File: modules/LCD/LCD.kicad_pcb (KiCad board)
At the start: 2 copper layers, 40.6 x 40.6 mm, 11 parts, among them J1 Conn_01x10_Male, J2 Conn_01x10_Male

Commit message: LCD shield in work
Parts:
- removed H5, H6, H7, H8: MountingHole, MountingHole:MountingHole_3.2mm_M3
- added RV1: R_POT, Potentiometer_THT:Potentiometer_ACP_CA9-V10_Vertical, F.Cu at (72.4, 49.5)
- DS1: footprint Display:WC1602A -> CommonLibrary:WH1602-2-holes
- moved DS1 86.2 mm to (78.5, 31.2)
- moved H2 80.4 mm to (148.0, 29.2), turned to 90 degrees
- moved H4 78.7 mm to (73.0, 29.2), turned to 90 degrees
- moved H1 55.8 mm to (148.0, 62.2), turned to 90 degrees
- moved H3 53.3 mm to (73.0, 62.2), turned to 90 degrees
- moved J2 31.0 mm to (120.0, 29.2), turned to 90 degrees
- moved J1 14.8 mm to (78.1, 62.2), turned to 90 degrees
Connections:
- DS1 pad 1: Net-(DS1-Pad1) -> GND
- DS1 pad 15: Net-(DS1-Pad15) -> VCC
- DS1 pad 16: Net-(DS1-Pad16) -> GND
- DS1 pad 2: Net-(DS1-Pad2) -> VCC
- DS1 pad 5: Net-(DS1-Pad5) -> GND
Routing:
- net GND: track 0.00 -> 99.1 mm, vias 0 -> 2
- net /2: track 0.00 -> 72.9 mm
- net VCC: track 0.00 -> 70.1 mm
- net /7: track 0.00 -> 61.1 mm, vias 0 -> 2
- net /8: track 0.00 -> 48.4 mm
- net /9: track 0.00 -> 41.2 mm
- net /10: track 0.00 -> 33.2 mm
- net /11: track 0.00 -> 25.5 mm
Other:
- board size 40.6 x 40.6 mm -> 82.5 x 40.6 mm

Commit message: LCD is ready
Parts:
- RV1: footprint Potentiometer_THT:Potentiometer_ACP_CA9-V10_Vertical -> CommonLibrary:pot-5x5
- moved RV1 6.16 mm to (73.7, 43.5), turned to 270 degrees
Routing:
- net Net-(DS1-Pad3): track 0.00 -> 18.8 mm
- net VCC: track 70.1 -> 84.2 mm
- net GND: track 99.1 -> 111.7 mm
- net /2: track 72.9 -> 77.5 mm
- net /7: track 61.1 -> 61.6 mm

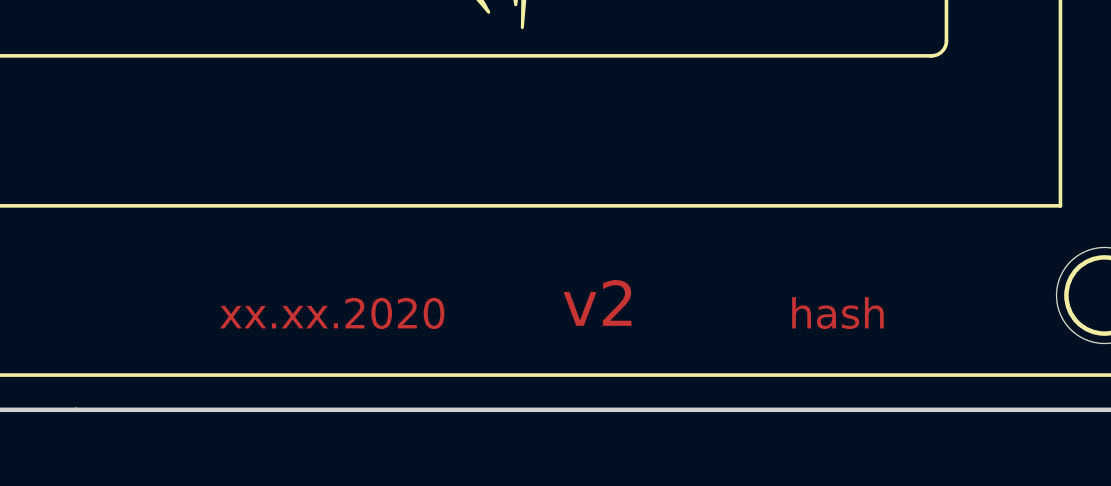
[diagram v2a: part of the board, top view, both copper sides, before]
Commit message: LCD. Add photomask in pdf.
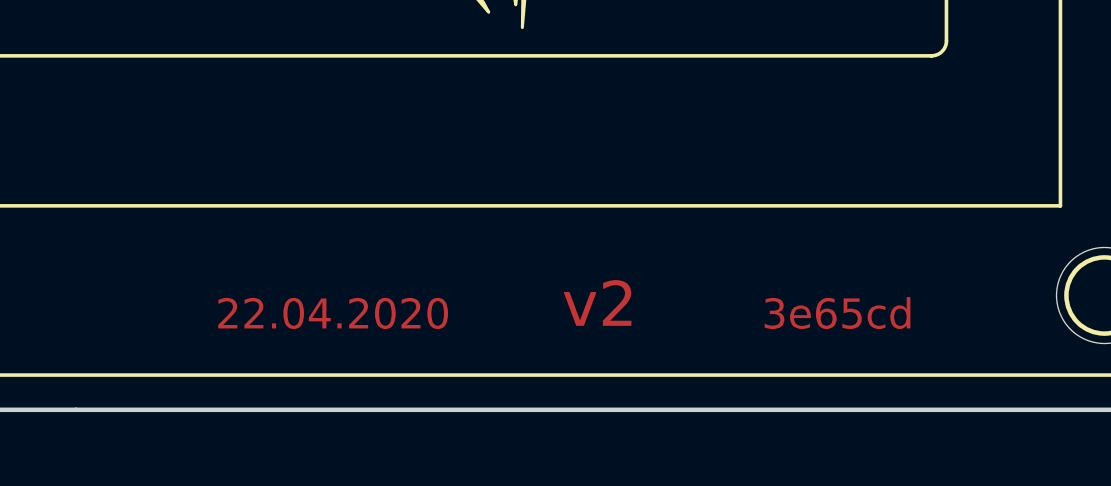
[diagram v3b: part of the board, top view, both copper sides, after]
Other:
- board text added: "22.04.2020"
- board text added: "3e65cd"
- board text removed: "hash"
- board text removed: "xx.xx.2020"
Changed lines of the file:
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@@
   )
   (setup
-    (last_trace_width 0.8)
+    (last_trace_width 0.25)
     (user_trace_width 0.6)
     (user_trace_width 0.8)
@@
     (visible_elements 7FFFFFFF)
     (pcbplotparams
-      (layerselection 0x010fc_ffffffff)
+      (layerselection 0x00000_fffffffe)
       (usegerberextensions false)
       (usegerberattributes false)
@@
       (hpglpenspeed 20)
       (hpglpendiameter 15.000000)
-      (psnegative false)
+      (psnegative true)
       (psa4output false)
       (plotreference true)
@@
       (padsonsilk false)
       (subtractmaskfromsilk false)
-      (outputformat 1)
+      (outputformat 4)
       (mirror false)
       (drillshape 1)
       (scaleselection 1)
-      (outputdirectory ""))
+      (outputdirectory "pdf/"))
   )
   (net 0 "")
@@
       (net 10 GND))
   )
-  (gr_text hash (at 139.065 62.865) (layer F.Cu)
+  (gr_text 3e65cd (at 139.065 62.865) (layer F.Cu)
     (effects (font (size 1 1) (thickness 0.2)))
   )
@@
     (effects (font (size 1.5 1.5) (thickness 0.3)))
   )
-  (gr_text xx.xx.2020 (at 122.2375 62.865) (layer F.Cu)
+  (gr_text 22.04.2020 (at 122.2375 62.865) (layer F.Cu)
     (effects (font (size 1 1) (thickness 0.2)))
   )

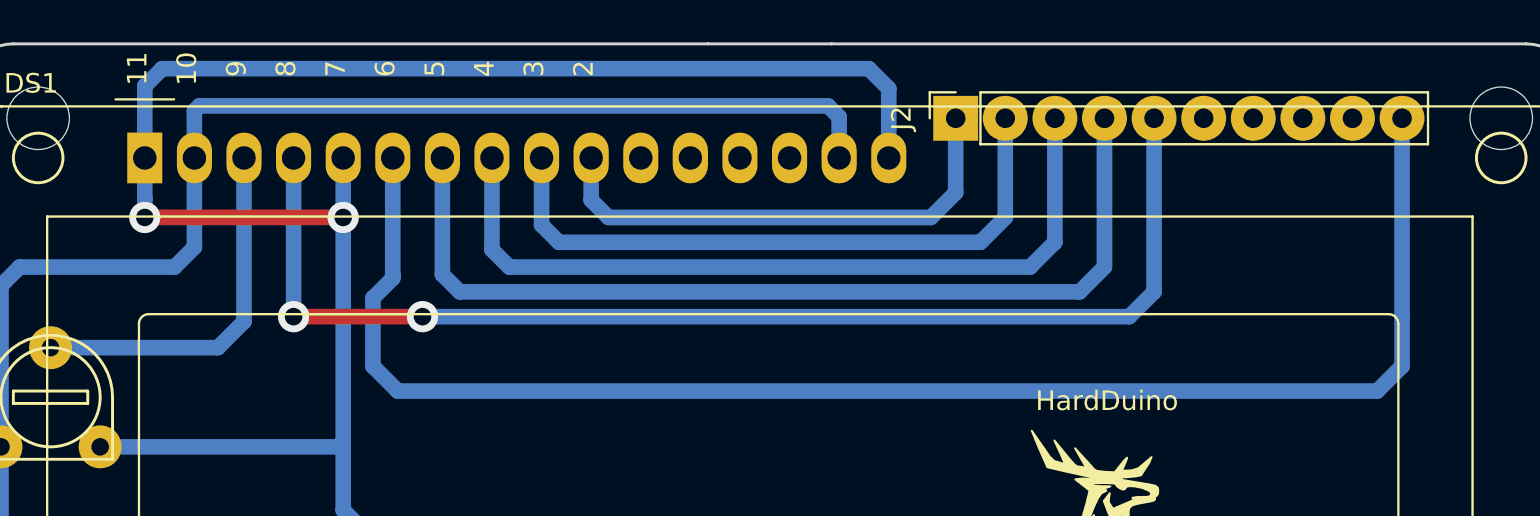
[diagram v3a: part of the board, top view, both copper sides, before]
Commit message: Fix LCD pins
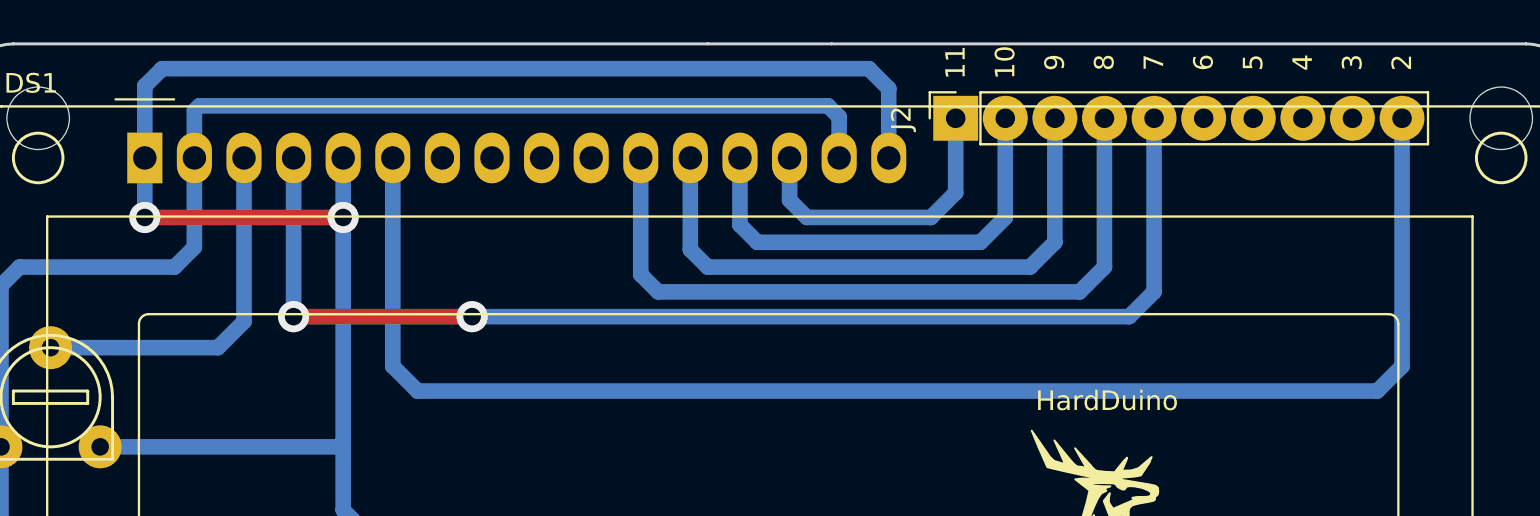
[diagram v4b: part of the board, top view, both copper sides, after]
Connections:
- DS1 pad 10: /11 -> Net-(DS1-Pad10)
- DS1 pad 11: Net-(DS1-Pad11) -> /8
- DS1 pad 12: Net-(DS1-Pad12) -> /9
- DS1 pad 13: Net-(DS1-Pad13) -> /10
- DS1 pad 14: Net-(DS1-Pad14) -> /11
- DS1 pad 7: /8 -> Net-(DS1-Pad7)
- DS1 pad 8: /9 -> Net-(DS1-Pad8)
- DS1 pad 9: /10 -> Net-(DS1-Pad9)
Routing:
- net /9: track 41.2 -> 30.6 mm
- net /8: track 48.4 -> 38.2 mm
- net /10: track 33.2 -> 23.0 mm
- net /11: track 25.5 -> 15.4 mm
- net /2: track 77.5 -> 76.1 mm

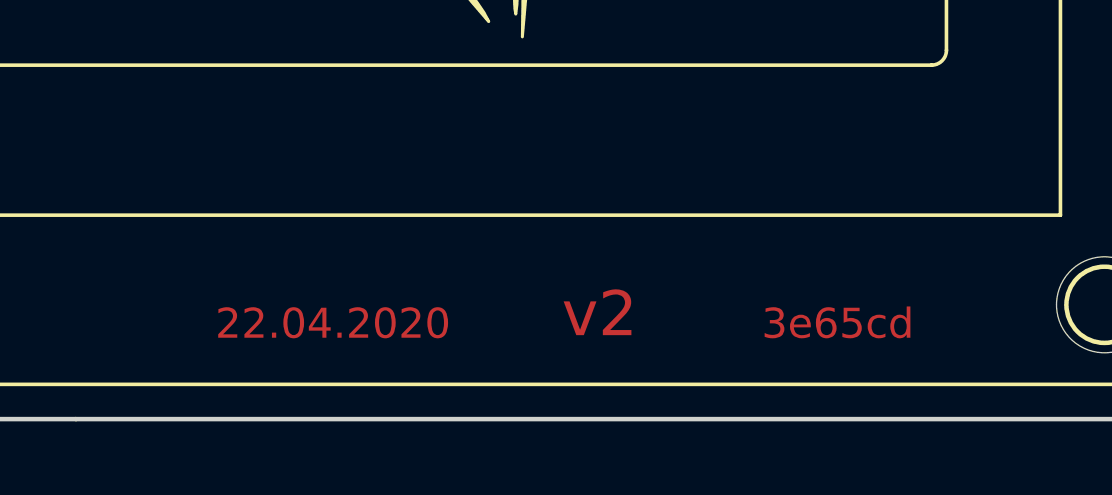
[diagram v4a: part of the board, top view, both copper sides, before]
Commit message: LCD. Add photomask in pdf.
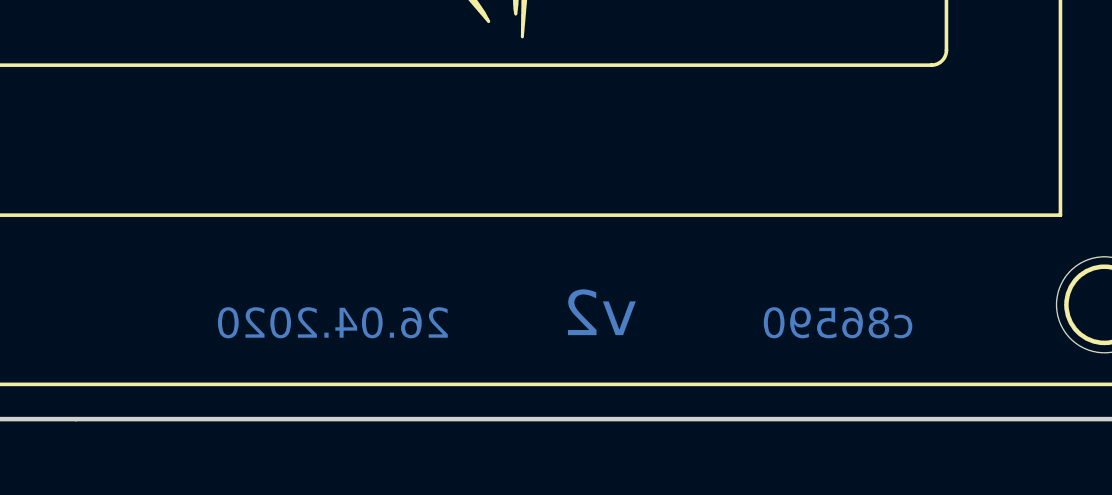
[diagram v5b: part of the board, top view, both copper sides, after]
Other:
- board text added: "26.04.2020"
- board text added: "c86590"
- board text removed: "22.04.2020"
- board text removed: "3e65cd"
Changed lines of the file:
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@@
   )
   (gr_line (start 107.315 25.4) (end 113.665 25.4) (layer Edge.Cuts) (width 0.15))
-  (gr_text 3e65cd (at 139.065 62.865) (layer F.Cu)
-    (effects (font (size 1 1) (thickness 0.2)))
+  (gr_text c86590 (at 139.065 62.865) (layer B.Cu)
+    (effects (font (size 1 1) (thickness 0.2)) (justify mirror))
   )
-  (gr_text v2 (at 131.1275 62.5475) (layer F.Cu)
-    (effects (font (size 1.5 1.5) (thickness 0.3)))
+  (gr_text v2 (at 131.1275 62.5475) (layer B.Cu)
+    (effects (font (size 1.5 1.5) (thickness 0.3)) (justify mirror))
   )
-  (gr_text 22.04.2020 (at 122.2375 62.865) (layer F.Cu)
-    (effects (font (size 1 1) (thickness 0.2)))
+  (gr_text 26.04.2020 (at 122.2375 62.865) (layer B.Cu)
+    (effects (font (size 1 1) (thickness 0.2)) (justify mirror))
   )
   (gr_poly (pts (xy 123.91 45.21) (xy 124.62 46.23) (xy 124.84 46.55) (xy 125.03 46.73) (xy 125.09 46.77) (xy 125.52 46.9) (xy 125.56 46.88) (xy 125.56 46.79) (xy 125.37 46.36) (xy 125.07 45.71) (xy 125.88 46.7) (xy 126.08 46.92) (xy 126.2 47.02) (xy 126.28 47.05) (xy 126.46 47.06) (xy 126.68 47.12) (xy 126.64 47) (xy 126.13 46.11) (xy 126.9 46.95) (xy 127.06 47.14) (xy 127.15 47.22) (xy 127.26 47.27) (xy 127.7 47.32) (xy 128.16 47.34) (xy 128.64 46.74) (xy 128.79 46.59) (xy 128.78 46.67) (xy 128.64 47) (xy 128.56 47.17) (xy 128.55 47.25) (xy 128.63 47.26) (xy 129.03 47.24) (xy 129.38 47.13) (xy 130.05 46.56) (xy 129.93 46.85) (xy 129.5 47.5) (xy 129.17 47.56) (xy 128.56 47.61) (xy 128.37 47.68) (xy 128.59 47.74) (xy 129.92 47.96) (xy 130.24 48.03) (xy 130.37 48.13) (xy 130.39 48.3) (xy 130.37 48.46) (xy 130.31 48.54) (xy 130.26 48.56) (xy 130.22 48.64) (xy 130.22 48.74) (xy 130.16 48.79) (xy 129.97 48.84) (xy 129.35 48.95) (xy 129.06 49.03) (xy 128.93 49.15) (xy 128.9 49.21) (xy 128.87 49.36) (xy 128.88 49.53) (xy 128.55 53.3) (xy 128.6 49.91) (xy 128.59 49.63) (xy 128.58 49.44) (xy 128.57 49.4) (xy 128.53 49.36) (xy 128.48 49.48) (xy 128.45 49.81) (xy 128.42 50.3) (xy 128.39 51.68) (xy 128.37 52.21) (xy 128.33 52.54) (xy 128.3 52.36) (xy 128.27 51.68) (xy 128.27 50.8) (xy 128.25 49.58) (xy 128.09 49.62) (xy 127.98 49.62) (xy 127.91 49.57) (xy 127.84 49.44) (xy 127.6 48.81) (xy 127.91 48.41) (xy 127.87 48.64) (xy 127.86 48.8) (xy 127.86 48.87) (xy 127.93 49) (xy 128.08 49.21) (xy 128.99 48.82) (xy 129.12 48.75) (xy 129.17 48.69) (xy 129.06 48.65) (xy 129.27 48.61) (xy 129.79 48.6) (xy 129.91 48.58) (xy 130 48.53) (xy 130.03 48.47) (xy 130 48.35) (xy 129.84 48.25) (xy 129.57 48.14) (xy 129.17 48.06) (xy 128.93 48.05) (xy 128.79 48.07) (xy 128.74 48.11) (xy 128.67 48.21) (xy 128.62 48.22) (xy 128.56 48.22) (xy 128.44 48.17) (xy 128.29 48.07) (xy 128.25 48.01) (xy 128.24 47.97) (xy 128.18 47.94) (xy 128.1 47.91) (xy 127.61 47.89) (xy 127.16 47.9) (xy 127.02 47.92) (xy 126.9 47.95) (xy 126.92 47.99) (xy 127.13 48.03) (xy 127.43 48.05) (xy 127.94 48.06) (xy 127.52 48.21) (xy 127.52 48.24) (xy 127.72 48.26) (xy 127.73 48.29) (xy 127.49 48.41) (xy 127.43 48.48) (xy 127.3 48.67) (xy 127.1 49.1) (xy 126.67 50.15) (xy 126.45 50.8) (xy 126.4 50.97) (xy 126.37 51.11) (xy 126.42 51.19) (xy 126.47 51.16) (xy 126.51 51.09) (xy 126.6 50.87) (xy 126.78 50.36) (xy 127.09 49.53) (xy 127.05 49.79) (xy 126.8 50.79) (xy 126.74 51) (xy 126.68 51.34) (xy 126.66 51.46) (xy 126.66 51.57) (xy 126.71 51.63) (xy 126.77 51.55) (xy 126.81 51.4) (xy 126.91 51.03) (xy 127.07 50.31) (xy 127.1 50.31) (xy 126.95 51.47) (xy 126.88 51.92) (xy 127.27 52.49) (xy 127.43 52.79) (xy 126.82 52.08) (xy 126.12 51.19) (xy 124.48 51.26) (xy 125.88 50.96) (xy 126.09 50.89) (xy 126.17 50.67) (xy 126.46 49.79) (xy 126.71 48.94) (xy 126.87 48.27) (xy 126.14 47.7) (xy 126.5 47.66) (xy 126.95 47.68) (xy 127.43 47.69) (xy 125.51 47.27) (xy 124.71 47.08) (xy 124.28 46.11)) (layer F.SilkS) (width 0.1))
@@
   (segment (start 127.635 36.83) (end 127.635 29.21) (width 0.8) (layer B.Cu) (net 17))
   (segment (start 104.775 38.1) (end 126.365 38.1) (width 0.8) (layer B.Cu) (net 17))
-  (segment (start 96.266 31.242) (end 96.266 31.642) (width 0.6) (layer B.Cu) (net 24))
   (segment (start 106.426 35.941) (end 107.315 36.83) (width 0.8) (layer B.Cu) (net 18))
   (segment (start 106.426 31.242) (end 106.426 35.941) (width 0.8) (layer B.Cu) (net 18))
@@
   (segment (start 82.2325 40.9575) (end 73.66 40.9575) (width 0.8) (layer B.Cu) (net 21))
   (segment (start 83.566 39.624) (end 82.2325 40.9575) (width 0.8) (layer B.Cu) (net 21))
+  (segment (start 96.266 31.242) (end 96.266 31.642) (width 0.6) (layer B.Cu) (net 24))
 )
